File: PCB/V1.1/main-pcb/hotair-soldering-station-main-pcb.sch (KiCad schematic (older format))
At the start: 94 parts, among them J1 230VAC_IN, J10 SOLD_IRON (r.2,54), J13 ICP (goldpin r2,54), J2 main-board-conn, J3 EARTH_GND, J4 24V_IN (NS-25 r2,54), J5 PSUPPLY (PWZ-02S r.3,96), J6 HOTAIR_FAN (JST r,2,54), J7 HOTAIR_MEAS (JST r.2,5), J8 HOTAIR_HEATER (PWZ-02S r.3,96)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

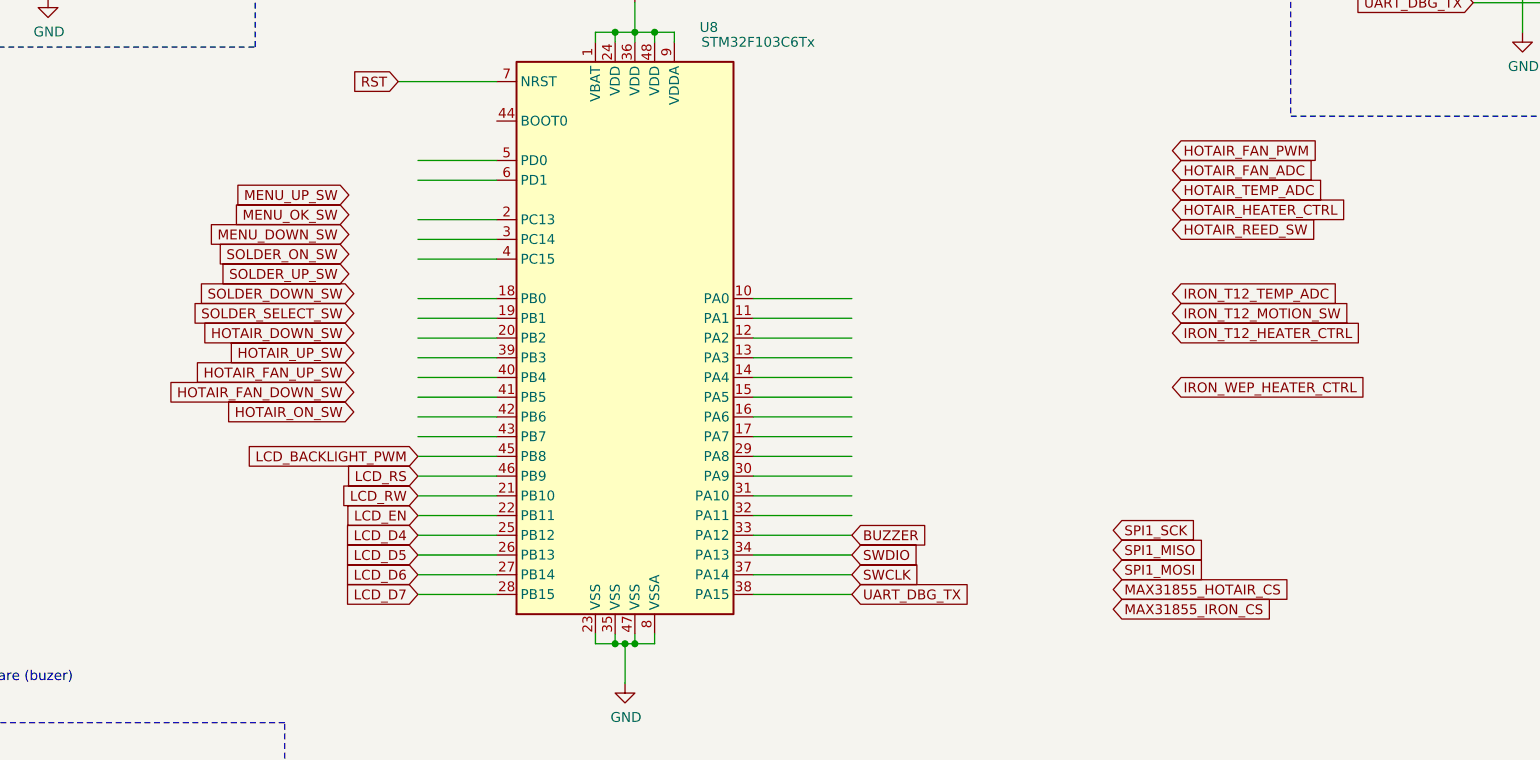
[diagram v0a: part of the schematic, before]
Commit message: Pin assign to new STM32F103, front panel design to new case
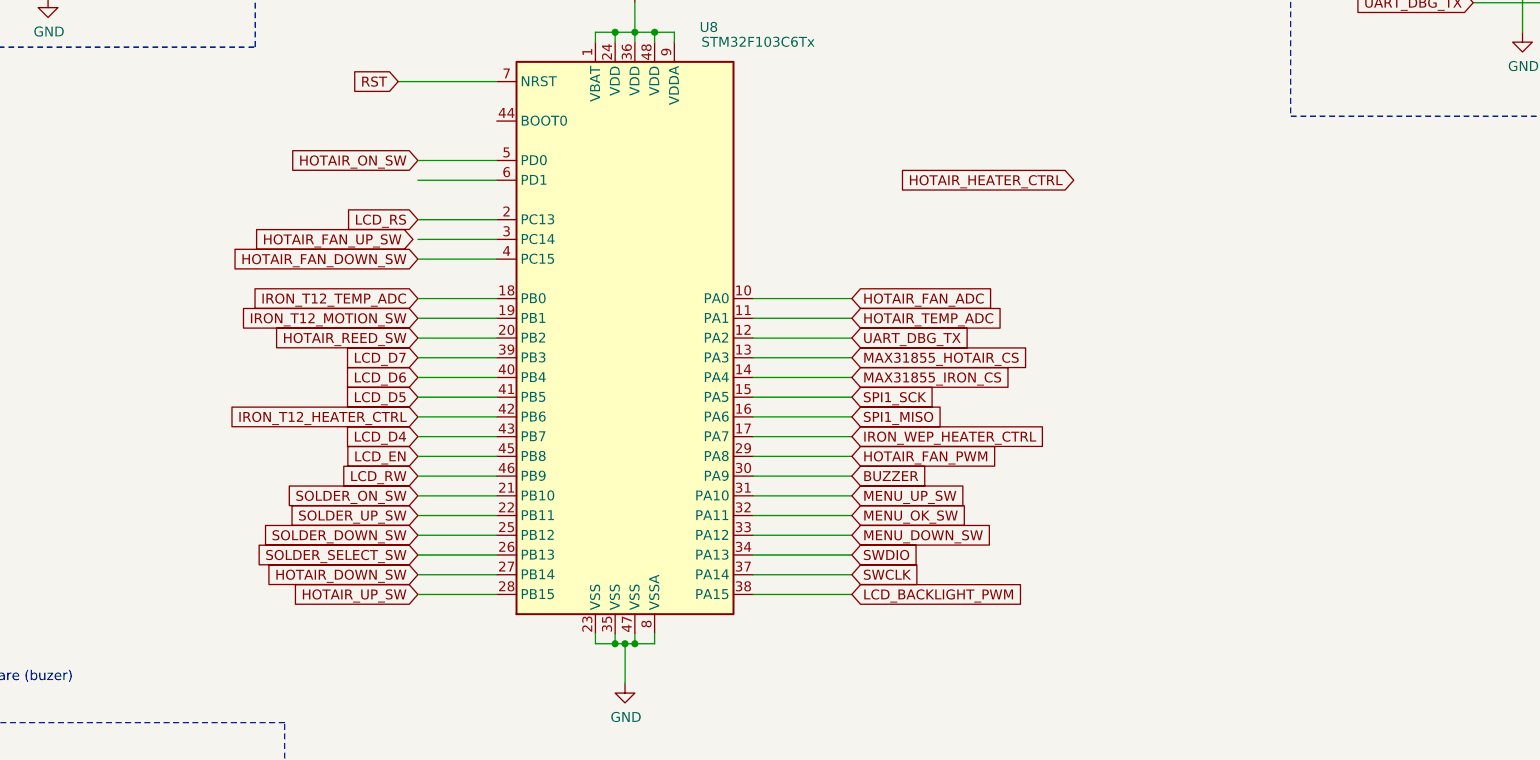
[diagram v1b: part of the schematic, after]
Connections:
- net labels removed: SPI1_MOSI
